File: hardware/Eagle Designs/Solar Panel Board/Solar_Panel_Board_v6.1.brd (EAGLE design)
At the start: 82.4 x 96.7 mm, 37 parts, among them J1 MOLEX_503763-0291MOLEX_503763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, J2 MOLEX_503763-0491MOLEX_503763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, J3 MOLEX_503763-0291MOLEX_503763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, U1 TMP36GSZ

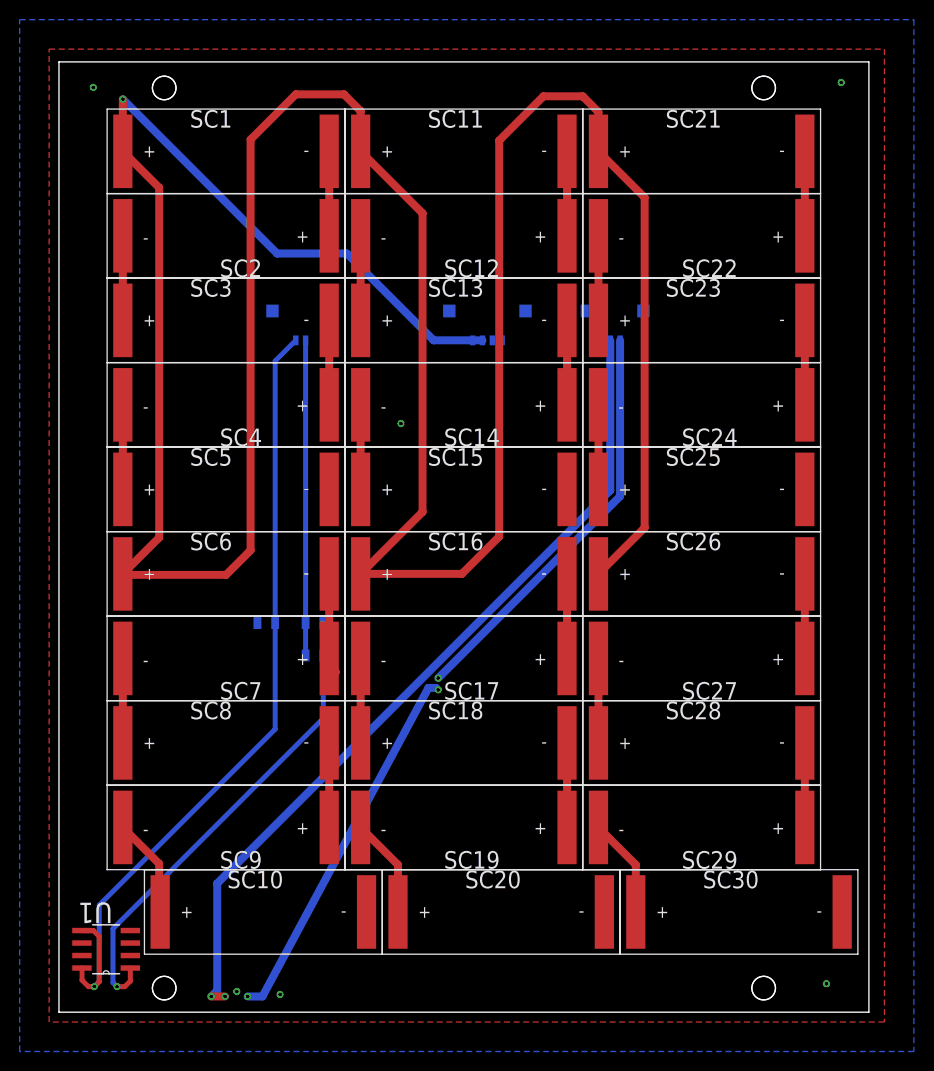
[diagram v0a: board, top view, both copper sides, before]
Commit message: Updated solar panel board temp sensor circuit
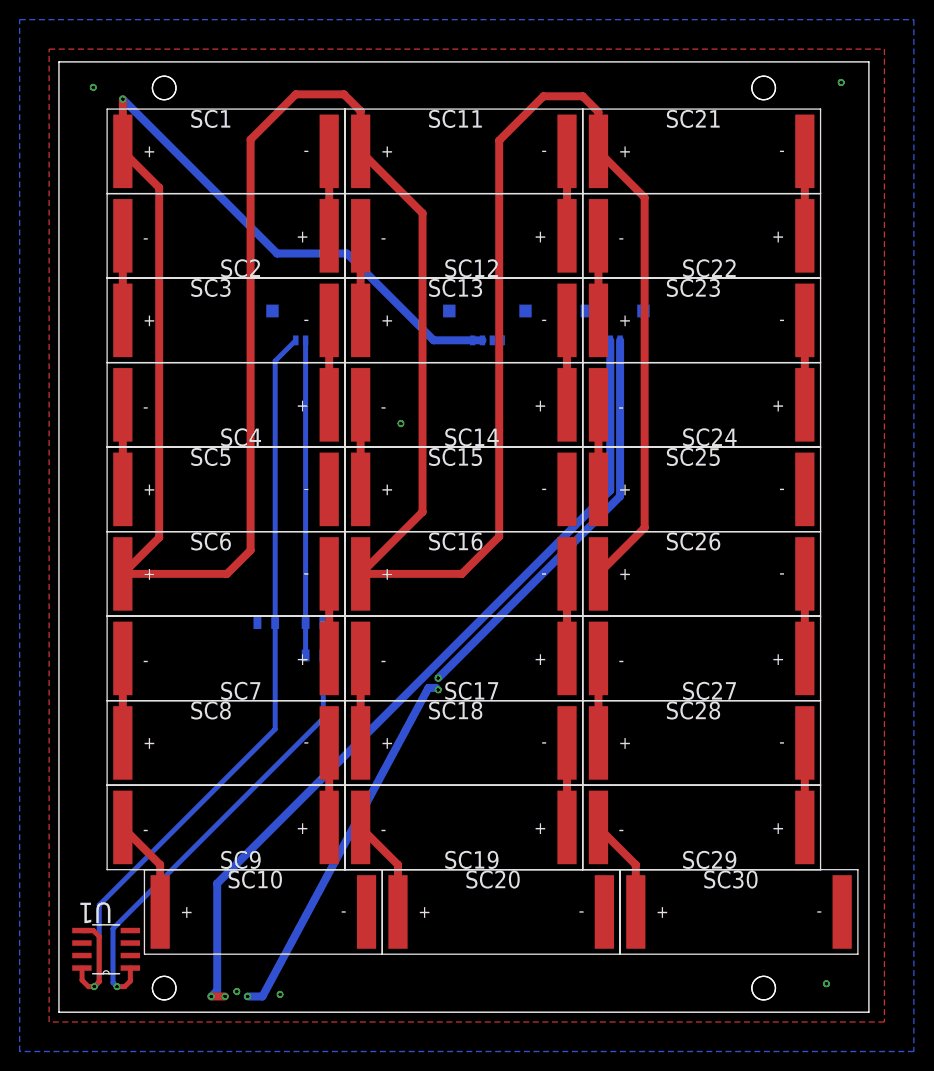
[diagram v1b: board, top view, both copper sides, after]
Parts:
- R1: value 27k -> 45.3k
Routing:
- net N$17: track 10.3 -> 8.60 mm
- net N$7: track 9.44 -> 8.60 mm
- net N$4: track 9.34 -> 8.60 mm
- net VCC: track 338.9 -> 339.5 mm
- net N$11: track 10.7 -> 10.2 mm
- net N$5: track 9.14 -> 8.60 mm
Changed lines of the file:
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@@
 <layers>
 <layer number="1" name="Top" color="4" fill="1" visible="yes" active="yes"/>
-<layer number="2" name="Route2" color="16" fill="1" visible="no" active="yes"/>
-<layer number="3" name="Route3" color="17" fill="1" visible="no" active="yes"/>
+<layer number="2" name="Route2" color="16" fill="1" visible="yes" active="yes"/>
+<layer number="3" name="Route3" color="17" fill="1" visible="yes" active="yes"/>
 <layer number="4" name="Route4" color="18" fill="1" visible="no" active="no"/>
 <layer number="5" name="Route5" color="19" fill="1" visible="no" active="no"/>
@@
 <attribute name="NAME" x="65.517" y="12.613" size="1.778" layer="25"/>
 </element>
-<element name="R1" library="HSFL_Main_Library" package="0805" value="27k" x="26" y="36.3" smashed="yes" rot="MR180">
+<element name="R1" library="HSFL_Main_Library" package="0805" value="45.3k" x="26" y="36.3" smashed="yes" rot="MR180">
 <attribute name="NAME" x="24.222" y="35.2205" size="0.8128" layer="26" font="vector" ratio="15" rot="SMR180"/>
 <attribute name="VALUE" x="24.222" y="38.3955" size="0.8128" layer="28" font="vector" ratio="15" rot="SMR180"/>
@@
 <wire x1="81.254" y1="5.054" x2="81.016" y2="4.816" width="0.3" layer="2"/>
 <wire x1="70.111025" y1="91.6" x2="81.054" y2="91.6" width="0.3" layer="2"/>
-<wire x1="81.016" y1="4.816" x2="70.027025" y2="4.816" width="0.3" layer="2"/>
-<wire x1="70.016" y1="4.816" x2="67.6" y2="2.4" width="0.3" layer="2"/>
-<wire x1="67.6" y1="2.4" x2="24.4" y2="2.4" width="0.3" layer="2"/>
-<wire x1="24.4" y1="2.4" x2="23.8" y2="3" width="0.3" layer="2"/>
+<wire x1="70.027025" y1="4.816" x2="81.016" y2="4.816" width="0.3" layer="2"/>
+<wire x1="23.8" y1="3" x2="24.4" y2="2.4" width="0.3" layer="2"/>
 <wire x1="23.8" y1="3" x2="14.4" y2="3" width="0.3" layer="2"/>
 <wire x1="14.4" y1="3" x2="11.8" y2="5.6" width="0.3" layer="2"/>
@@
 <wire x1="16.1" y1="13.1" x2="16.1" y2="2.2" width="0.8128" layer="16"/>
 <wire x1="16.1" y1="13.1" x2="56.1" y2="53.1" width="0.8128" layer="16"/>
-<wire x1="70.027025" y1="4.816" x2="70.016" y2="4.816" width="0" layer="19" extent="2-2"/>
+<wire x1="67.611025" y1="2.4" x2="70.027025" y2="4.816" width="0.3" layer="2"/>
+<wire x1="24.4" y1="2.4" x2="67.611025" y2="2.4" width="0.3" layer="2"/>
 </signal>
 <signal name="GND">
@@
 <wire x1="30.7" y1="91.7" x2="29" y2="93.4" width="0.8128" layer="1"/>
 <wire x1="29" y1="93.4" x2="24.1" y2="93.4" width="0.8128" layer="1"/>
-<wire x1="19.5" y1="88.8" x2="19.5" y2="47" width="0.8128" layer="1"/>
-<wire x1="19.5" y1="47" x2="17" y2="44.5" width="0.8128" layer="1"/>
-<wire x1="17" y1="44.5" x2="7.2" y2="44.5" width="0.8128" layer="1"/>
+<wire x1="19.5" y1="47" x2="19.5" y2="88.8" width="0.8128" layer="1"/>
 <wire x1="24.1" y1="93.4" x2="19.5" y2="88.8" width="0.8128" layer="1"/>
 <wire x1="30.7" y1="87.6" x2="37" y2="81.3" width="0.8128" layer="1"/>
@@
 <wire x1="59.6" y1="82.9" x2="54.9" y2="87.6" width="0.8128" layer="1"/>
 <wire x1="59.6" y1="49.3" x2="59.6" y2="82.9" width="0.8128" layer="1"/>
-<wire x1="7.2" y1="44.5" x2="6.5" y2="44.6" width="0" layer="19" extent="1-1"/>
+<wire x1="6.5" y1="44.6" x2="17.1" y2="44.6" width="0.8128" layer="1"/>
+<wire x1="17.1" y1="44.6" x2="19.5" y2="47" width="0.8128" layer="1"/>
 </signal>
 <signal name="VS+">
@@
 <contactref element="SC2" pad="-"/>
 <contactref element="SC3" pad="+"/>
-<wire x1="6.5" y1="79" x2="6.5" y2="70" width="0.8128" layer="1"/>
-<wire x1="6.5" y1="70" x2="6.4" y2="69.9" width="0.8128" layer="1"/>
-<wire x1="6.4" y1="69.9" x2="6.5" y2="70.4" width="0" layer="19" extent="1-1"/>
+<wire x1="6.5" y1="70.4" x2="6.5" y2="79" width="0.8128" layer="1"/>
 </signal>
 <signal name="N$6">
@@
 <contactref element="SC12" pad="+"/>
 <contactref element="SC11" pad="-"/>
-<wire x1="51.7" y1="87.6" x2="51.7" y2="78.1" width="0.8128" layer="1"/>
+<wire x1="51.7" y1="79" x2="51.7" y2="78.1" width="0.8128" layer="1"/>
 <wire x1="51.7" y1="78.1" x2="51.5" y2="77.9" width="0.8128" layer="1"/>
-<wire x1="51.5" y1="77.9" x2="51.7" y2="79" width="0" layer="19" extent="1-1"/>
+<wire x1="51.7" y1="79" x2="51.7" y2="87.6" width="0.8128" layer="1"/>
 </signal>
 <signal name="N$14">
@@
 <contactref element="SC8" pad="-"/>
 <contactref element="SC9" pad="+"/>
-<wire x1="27.5" y1="27.4" x2="27.5" y2="18.1" width="0.8128" layer="1"/>
-<wire x1="27.5" y1="18.1" x2="27.6" y2="18" width="0.8128" layer="1"/>
-<wire x1="27.6" y1="18" x2="27.5" y2="18.8" width="0" layer="19" extent="1-1"/>
+<wire x1="27.5" y1="18.8" x2="27.5" y2="27.4" width="0.8128" layer="1"/>
 </signal>
 <signal name="N$8">
@@
 <contactref element="SC3" pad="-"/>
 <contactref element="SC4" pad="+"/>
-<wire x1="27.5" y1="70.4" x2="27.5" y2="61.2" width="0.8128" layer="1"/>
-<wire x1="27.5" y1="61.2" x2="27.4" y2="61.1" width="0.8128" layer="1"/>
-<wire x1="27.4" y1="61.1" x2="27.5" y2="61.8" width="0" layer="19" extent="1-1"/>
+<wire x1="27.5" y1="61.8" x2="27.5" y2="70.4" width="0.8128" layer="1"/>
 </signal>
 <signal name="N$17">
 <contactref element="SC7" pad="+"/>
 <contactref element="SC6" pad="-"/>
-<wire x1="27.5" y1="44.6" x2="27.5" y2="35.3" width="0.8128" layer="1"/>
-<wire x1="27.5" y1="35.3" x2="28.2" y2="34.6" width="0.8128" layer="1"/>
-<wire x1="28.2" y1="34.6" x2="27.5" y2="36" width="0" layer="19" extent="1-1"/>
+<wire x1="27.5" y1="44.6" x2="27.5" y2="36" width="0.8128" layer="1"/>
 </signal>
 <signal name="N$11">
 <contactref element="SC10" pad="+"/>
 <contactref element="SC9" pad="-"/>
-<wire x1="6.5" y1="18.8" x2="10.2" y2="15.1" width="0.8128" layer="1"/>
-<wire x1="10.2" y1="15.1" x2="10.2" y2="9.6" width="0.8128" layer="1"/>
-<wire x1="10.2" y1="9.6" x2="10.3" y2="10.2" width="0" layer="19" extent="1-1"/>
+<wire x1="6.5" y1="18.8" x2="10.3" y2="15" width="0.8128" layer="1"/>
+<wire x1="10.3" y1="15" x2="10.3" y2="10.2" width="0.8128" layer="1"/>
 </signal>
 <signal name="N$20">
